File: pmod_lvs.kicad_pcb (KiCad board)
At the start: 2 copper layers, 39.6 x 16.8 mm, 29 parts, among them J1 PMOD_Socket, J2 PMOD_Header, J3 HV_connector, Q1 BSS138, Q2 BSS138, Q3 BSS138, Q4 BSS138, Q5 BSS138, Q6 BSS138, Q7 BSS138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

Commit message: Migrate to KiCad 6
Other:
- net class Default removed

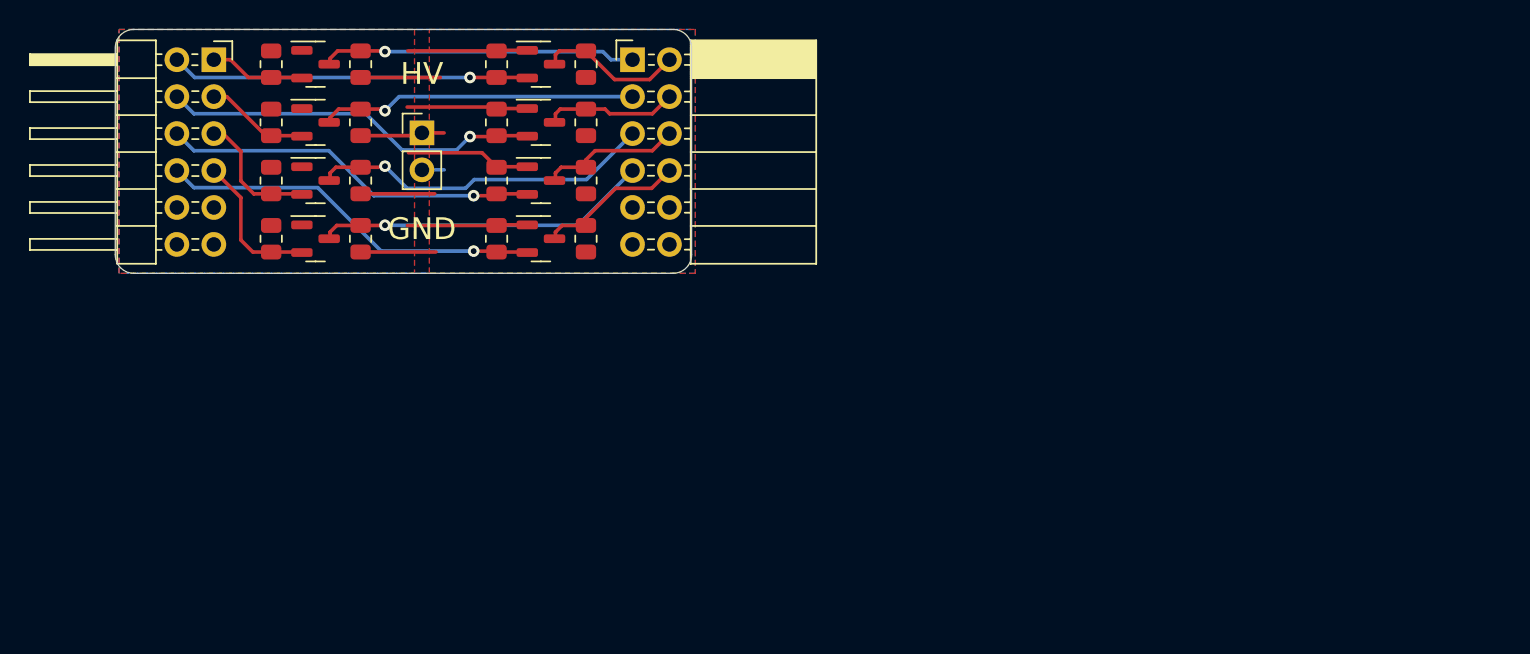
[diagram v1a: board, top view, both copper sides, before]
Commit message: Add IBOM
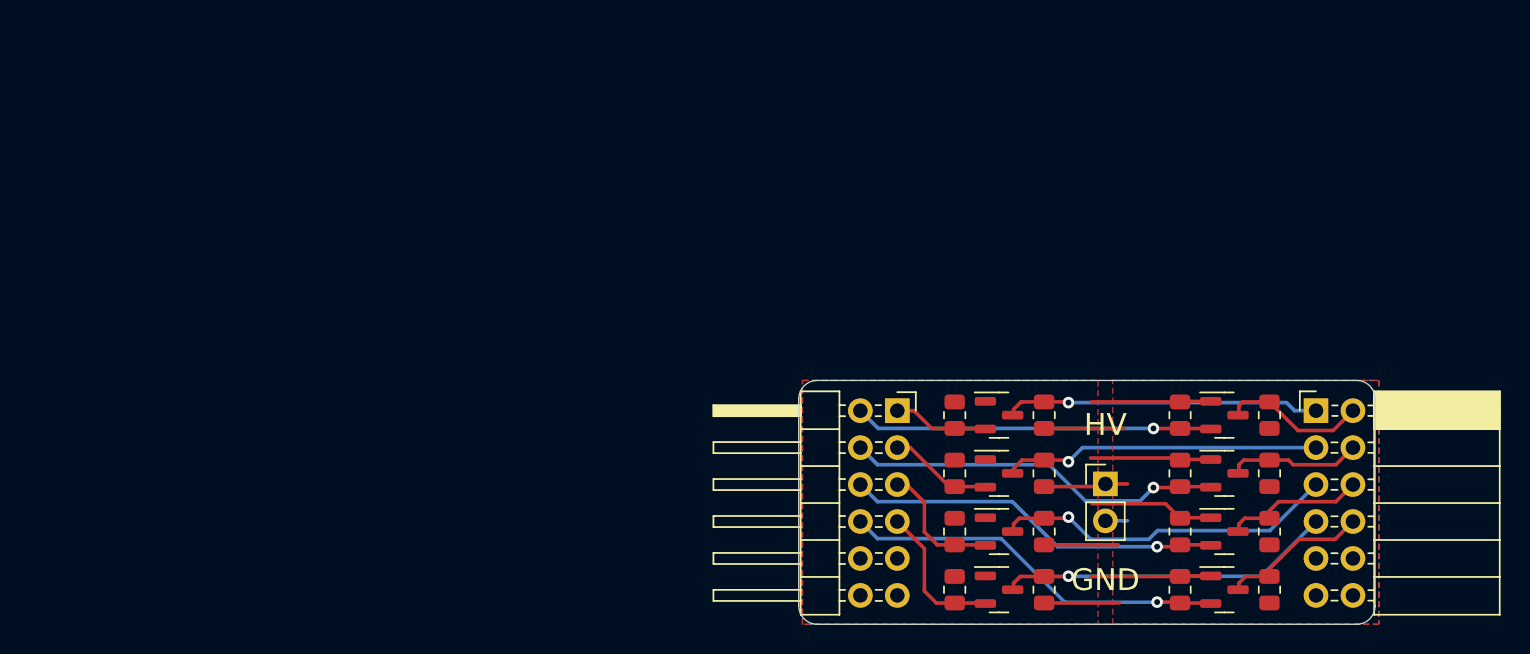
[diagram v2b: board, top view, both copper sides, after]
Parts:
- moved J1 52.8 mm to (166.4, 95.8)
- moved J2 52.8 mm to (137.6, 95.8)
- moved R10 52.8 mm to (163.2, 96.1)
- moved R12 52.8 mm to (163.2, 100.1)
- moved R14 52.8 mm to (163.2, 104.1)
- moved R16 52.8 mm to (163.2, 108.1)
- moved R2 52.8 mm to (147.7, 96.1)
- moved R4 52.8 mm to (147.7, 100.1)
- moved R6 52.8 mm to (147.7, 104.1)
- moved R8 52.8 mm to (147.7, 108.1)
- moved Q1 52.8 mm to (144.6, 96.1)
- moved Q2 52.8 mm to (144.6, 100.1)
- moved Q3 52.8 mm to (144.6, 104.1)
- moved Q4 52.8 mm to (144.6, 108.1)
- moved Q5 52.8 mm to (160.1, 96.1)
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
